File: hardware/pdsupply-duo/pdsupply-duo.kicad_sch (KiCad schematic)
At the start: 3 parts

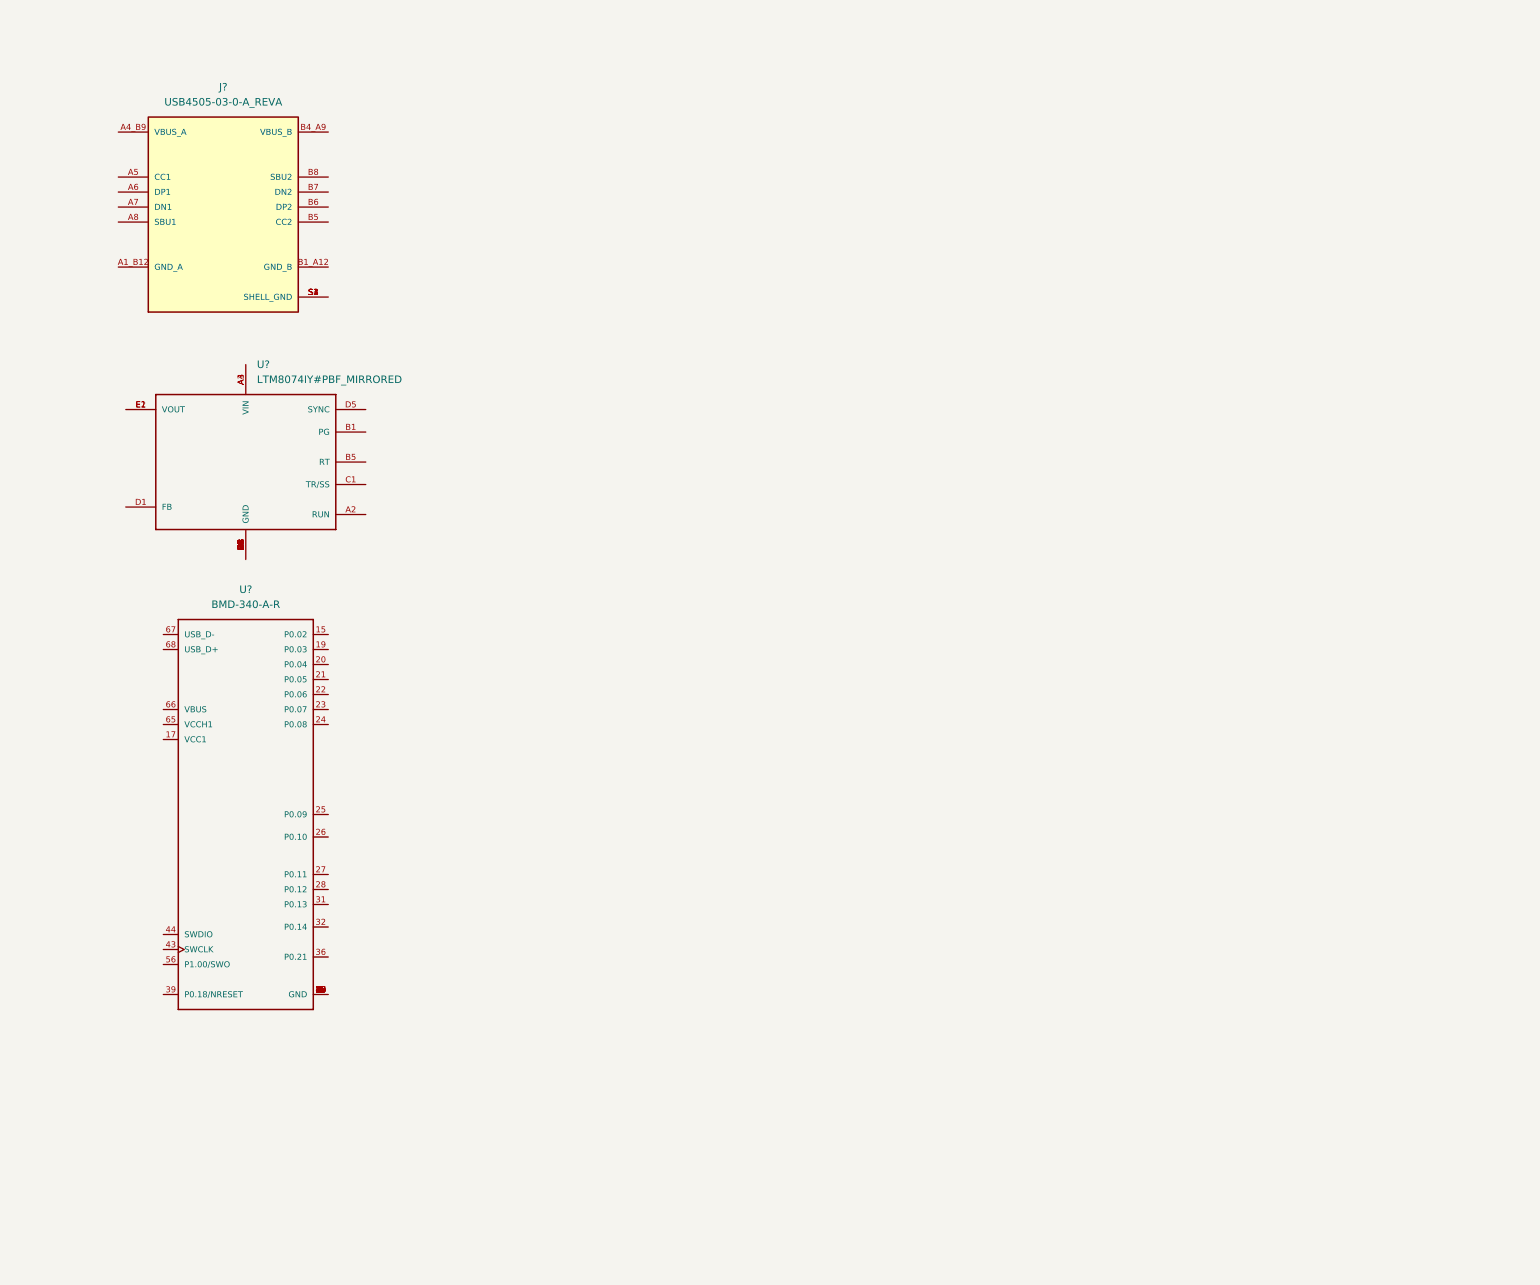
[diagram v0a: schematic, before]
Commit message: Added Power for digital hardware
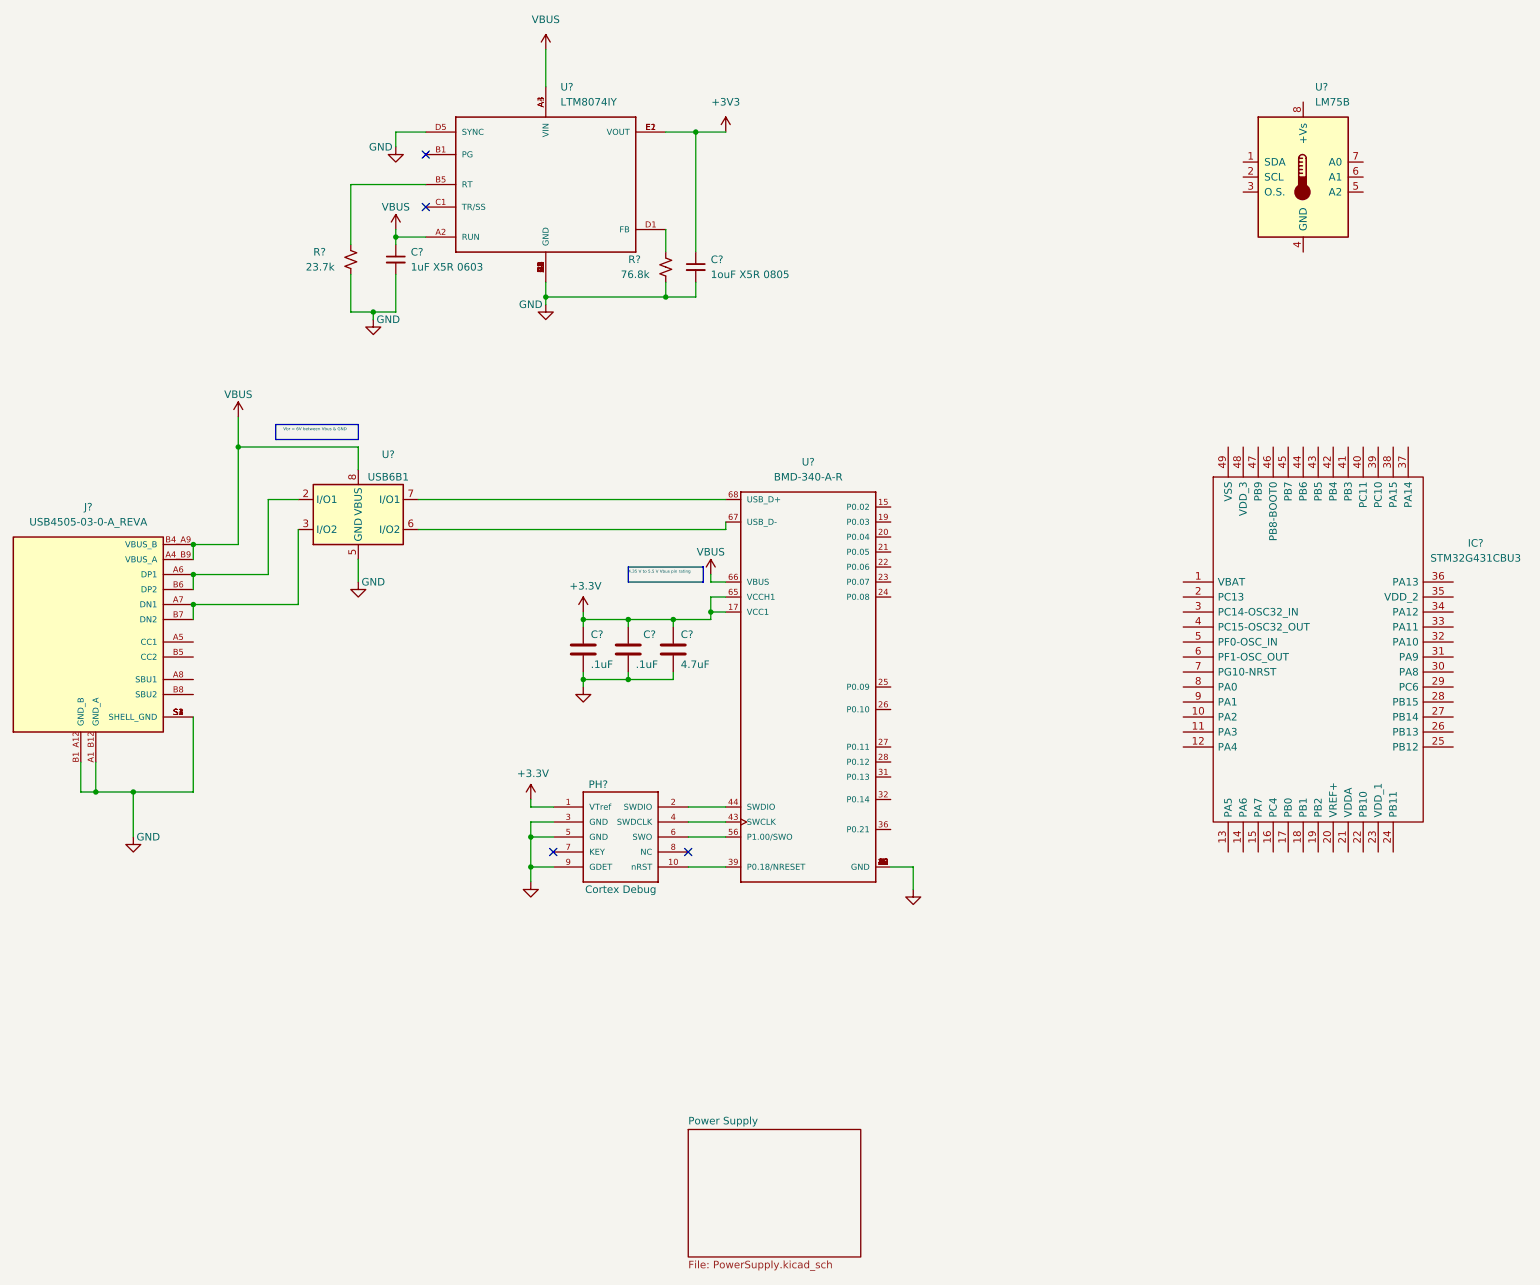
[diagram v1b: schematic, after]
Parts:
- added C? (x2): .1uF, Capacitor_SMD:C_0603_1608Metric, symbol Device:C
- added C?: 1uF X5R 0603, symbol Device:C_Small
- added C?: 1ouF X5R 0805, symbol Device:C_Small
- added C?: 4.7uF, Capacitor_SMD:C_0603_1608Metric, symbol Device:C
- added IC?: STM32G431CBU3, QFN50P700X700X65-49N-D, symbol STM32G431CBU3:STM32G431CBU3
- added PH?: FTSH-105-01-L-DV-K, FTSH-105-01-L-DV-K:SAMTEC_FTSH-105-01-L-DV-K, symbol FTSH-105-01-L-DV-K:FTSH-105-01-L-DV-K
- added R?: 23.7k, symbol Device:R_Small_US
- added R?: 76.8k, symbol Device:R_Small_US
- added U?: LM75B, symbol Sensor_Temperature:LM75B
- added U?: USB6B1, Package_SO:SOIC-8_3.9x4.9mm_P1.27mm, symbol Power_Protection:USB6B1
- U?: value LTM8074IY#PBF_MIRRORED -> LTM8074IY
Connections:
- net GND: now reaches U?.A1 (GND), U?.A5 (GND), U?.B2 (GND), U?.B3 (GND), U?.B4 (GND), U?.C2 (GND), U?.C3 (GND), U?.C4 (GND), U?.C5 (GND), U?.D2 (GND), U?.D3 (GND), U?.D4 (GND), U?.E3 (GND), U?.E4 (GND), U?.E5 (GND)
- net GND: now also J?.A1_B12 (GND_A), J?.B1_A12 (GND_B), J?.S1 (SHELL_GND), J?.S2 (SHELL_GND), J?.S3 (SHELL_GND), J?.S4 (SHELL_GND), U?.1 (GND), U?.16 (GND), U?.18 (GND), U?.2 (GND), U?.29 (GND), U?.3 (GND), U?.30 (GND), U?.4 (GND), U?.45 (GND), U?.46 (GND), U?.47 (GND), U?.5 (GND), U?.55 (GND), U?.D5 (SYNC), C?.2, C?.2, C?.2, C?.2, C?.2, PH?.3 (GND), PH?.5 (GND), PH?.9 (GDET), R?.2, R?.2, U?.4 (GND), U?.5 (GND)
- net VBUS: now reaches U?.A2 (RUN)
- net VBUS: now also J?.A4_B9 (VBUS_A), J?.B4_A9 (VBUS_B), U?.66 (VBUS), U?.A3 (VIN), U?.A4 (VIN), C?.1, U?.1 (VBUS), U?.8 (VBUS)
- net at U?.B5 (RT): now also R?.1
- net at U?.D1 (FB): now also R?.1
- net +3V3: now reaches U?.E1 (VOUT), U?.E2 (VOUT)
- net +3V3: now also U?.17 (VCC1), U?.65 (VCCH1), C?.1, C?.1, C?.1, C?.1, PH?.1 (VTref)
- net at U?.39 (P0.18/NRESET): now also PH?.10 (nRST)
- net at U?.43 (SWCLK): now also PH?.4 (SWDCLK)
- net at U?.44 (SWDIO): now also PH?.2 (SWDIO)
- net at U?.56 (P1.00/SWO): now also PH?.6 (SWO)
- net at U?.67 (USB_D-): now also U?.6 (I/O2)
- net at U?.68 (USB_D+): now also U?.7 (I/O1)
- net at J?.A6 (DP1): now also J?.B6 (DP2), U?.2 (I/O1)
- net at J?.A7 (DN1): now also J?.B7 (DN2), U?.3 (I/O2)
- no-connect marks 0 -> 4
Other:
- added sheet Power Supply (PowerSupply.kicad_sch)
- note added: "4.35 V to 5.5 V Vbus pin rating"
- note added: "Vbr = 6V between Vbus & GND"
- moved on the sheet: J?, U?

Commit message: Added usb PD interface
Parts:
- removed C? (x2): .1uF, Capacitor_SMD:C_0603_1608Metric, symbol Device:C
- removed C?: 4.7uF, Capacitor_SMD:C_0603_1608Metric, symbol Device:C
- removed IC?: STM32G431CBU3, QFN50P700X700X65-49N-D, symbol STM32G431CBU3:STM32G431CBU3
- removed PH?: FTSH-105-01-L-DV-K, FTSH-105-01-L-DV-K:SAMTEC_FTSH-105-01-L-DV-K, symbol FTSH-105-01-L-DV-K:FTSH-105-01-L-DV-K
- removed U?: USB6B1, Package_SO:SOIC-8_3.9x4.9mm_P1.27mm, symbol Power_Protection:USB6B1
- removed U?: BMD-340-A-R, RIGADO_BMD-340-A-R, symbol BMD-340-A-R:BMD-340-A-R
- added C? (x3): 1uF, symbol Device:C_Small
- added C?: 0.1uF, symbol Device:C_Small
- added C? (x2): .1uF, Capacitor_SMD:C_0603_1608Metric, symbol Device:C
- added C?: 4.7uF, Capacitor_SMD:C_0603_1608Metric, symbol Device:C
- added D? (x2): 25V, symbol Device:D_Schottky_Small
- added PH?: FTSH-105-01-L-DV-K, FTSH-105-01-L-DV-K:SAMTEC_FTSH-105-01-L-DV-K, symbol FTSH-105-01-L-DV-K:FTSH-105-01-L-DV-K
- added Q?: STL6P3LLH6, TRANS_STL6P3LLH6, symbol STL6P3LLH6:STL6P3LLH6
- added R?: 100, symbol Device:R_Small_US
- added R? (x4): 100k, symbol Device:R_Small_US
- added R? (x4): 2.2k, symbol Device:R_Small_US
- added R? (x2): 1K, symbol Device:R_Small_US
- added R?: 22K, symbol Device:R_Small_US
- added U3: BMD-340-A-R, RIGADO_BMD-340-A-R, symbol BMD-340-A-R:BMD-340-A-R
- added U4: STUSB4500QTR, Package_DFN_QFN:QFN-24-1EP_4x4mm_P0.5mm_EP2.7x2.7mm, symbol Interface_USB:STUSB4500QTR
- C1: renamed from C?; value 1uF X5R 0603 -> 1uF
- C5: renamed from C?; value 1ouF X5R 0805 -> 10uF X5R 0805
- gave numbers to parts that had none: 5
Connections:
- net +3V3: now also U4.8 (+Vs), C?.1, C?.1, C?.1, PH?.1 (VTref), R?.1, R?.1, R?.1, R?.1, U3.17 (VCC1), U3.65 (VCCH1), U4.22 (VSYS)
- net GND: now also U4.4 (GND), C?.2, C?.2, C?.2, C?.2, C?.2, C?.2, D?.2 (A), D?.2 (A), PH?.3 (GND), PH?.5 (GND), PH?.9 (GDET), R?.2, R?.2, R?.2, U3.1 (GND), U3.16 (GND), U3.18 (GND), U3.2 (GND), U3.29 (GND), U3.3 (GND), U3.30 (GND), U3.4 (GND), U3.45 (GND), U3.46 (GND), U3.47 (GND), U3.5 (GND), U3.55 (GND), U4.10 (GND)
- net VBUS: now also C?.1, Q?.1, Q?.2, Q?.3, R?.1, R?.1, U3.66 (VBUS), U4.24 (VDD)
- net MAIN_SDA: now reaches U4.1 (SDA)
- net MAIN_SDA: now also R?.2
- net MAIN_SCL: now reaches U4.2 (SCL)
- net MAIN_SCL: now also R?.2
- net at U4.5 (A2): now also U4.6 (A1), U4.7 (A0), R?.1
- net at J1.A6 (DP1): no longer J1.B6 (DP2)
- net at J1.A7 (DN1): no longer J1.B7 (DN2)
- net CC1: now reaches J1.A5 (CC1)
- net CC1: now also D?.1 (K), U4.1 (CC1DB), U4.2 (CC1)
- net CC2: now reaches J1.B5 (CC2)
- net CC2: now also D?.1 (K), U4.4 (CC2), U4.5 (CC2DB)
- new net: C?.2, R?.1
- new net: Q?.4, R?.2, R?.2, R?.2
- new net: R?.2, U4.9 (DISCH)
- new net: R?.2, U4.18 (VBUS_VS_DISCH)
- new net: C?.1, U4.23 (VREG_2V7)
- new net: R?.1, U4.16 (VBUS_EN_SNK)
- new net: R?.1, U4.12 (ADDR0), U4.13 (ADDR1)
- new net: C?.1, U4.21 (VREG_1V2)
- new net: PH?.10 (nRST), U3.39 (P0.18)
- new net: PH?.2 (SWDIO), U3.44 (SWDIO)
- new net: PH?.4 (SWDCLK), U3.43 (SWCLK)
- new net: PH?.6 (SWO), U3.56 (P1.00)
- new net POK2: U4.20 (POWER_OK2)
- new net POK3: U4.14 (POWER_OK3)
- new net STUSB_RESET: R?.1, U4.6 (RESET)
- new net STUSB_SCL: R?.2, U4.7 (SCL)
- new net STUSB_SDA: R?.2, U4.8 (SDA)
- new net VS: C?.1, Q?.5_8, R?.1
- no-connect marks 4 -> 15
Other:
- sheet Power Supply ports: added ADDR_DIGIPOT; removed none
- note added: "i2c addr 0x48"
- note removed: "4.35 V to 5.5 V Vbus pin rating"
- note removed: "Vbr = 6V between Vbus & GND"
- moved on the sheet: C1, C5, R1, R2, U1, U4

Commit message: SCH 85% done
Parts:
- added R? (x2): devider, symbol Device:R_Small_US
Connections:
- net GND: now also R?.2
- net MAIN_SCL: now also U3.61 (P1.12)
- net MAIN_SDA: now also U3.62 (P1.13)
- net POK2: now also U3.14 (P0.01)
- net POK3: now also U3.13 (P0.00)
- net STUSB_RESET: now also U3.15 (P0.02)
- net STUSB_SCL: now also U3.7 (P0.26)
- net STUSB_SDA: now also U3.9 (P0.28)
- net VS: now also R?.1
- net Vs_sense: now reaches U3.19 (P0.03)
- net Vs_sense: now also R?.1, R?.2
- net Current1: now reaches U3.20 (P0.04)
- net Current2: now reaches U3.21 (P0.05)
- net Sync1: now reaches U3.25 (P0.09)
- net Sync2: now reaches U3.27 (P0.11)
- net Reset1: now reaches U3.63 (P1.14)
- net Reset2: now reaches U3.64 (P1.15)
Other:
- added sheet Power Supply1 (PowerSupply.kicad_sch)
- sheet Power Supply ports: added Isense, RESET_DIGIPOT, SYNC, Vout; removed none
- note added: "i2c addr 0x2C"
- note added: "i2c addr 0x2F"
- moved on the sheet: C?, D?, PH?, R?, U3, U4
